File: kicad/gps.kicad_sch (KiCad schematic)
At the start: 68 parts, among them J1 Bus_PCI_Express_x1, J2 USB_C_Receptacle_USB2.0_16P, J3 Conn_01x02, J4 USB_C_Receptacle_USB2.0_16P, Q1 IRLML6344, U2 W25Q128JVP, U3 MCP25625T-E/ML, U4 RP2040, U5 NEO-M9N, X1 ABM8-272-T3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

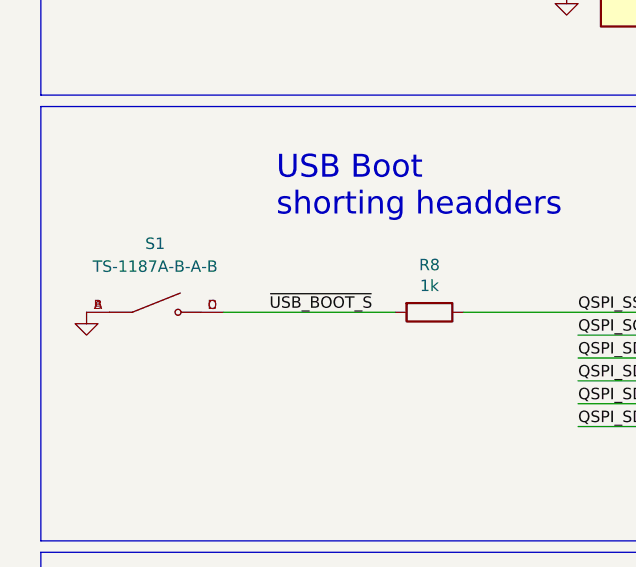
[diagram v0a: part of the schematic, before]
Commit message: Fix Battery Position
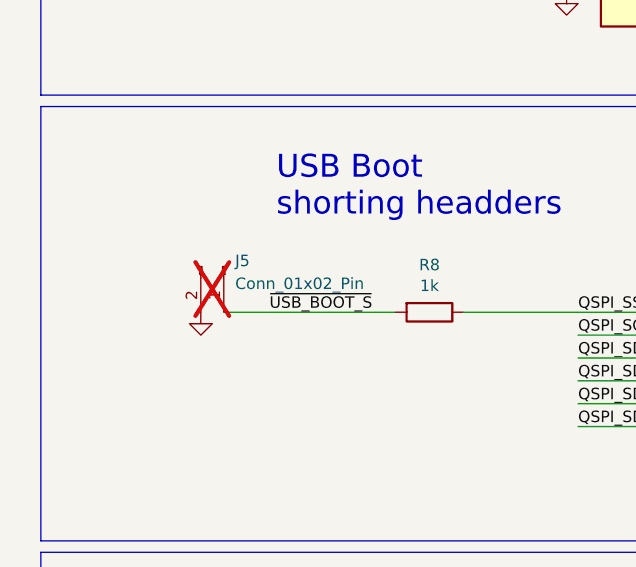
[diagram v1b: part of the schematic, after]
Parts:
- removed S1: TS-1187A-B-A-B, GPSLIB:SW_TS-1187A-B-A-B, symbol TS-1187A-B-A-B:TS-1187A-B-A-B
- added J5: Conn_01x02_Pin, Connector_PinHeader_2.54mm:PinHeader_1x02_P2.54mm_Vertical, symbol Connector:Conn_01x02_Pin
- BAT1: JLC Link https://jlcpcb.com/partdetail/C238096 -> https://jlcpcb.com/partdetail/Keystone-2998TR/C6078169; LCSC Part # C238096 -> C6078169; Manufacturer Part Number 2998 -> 2998TR
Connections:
- net GND: now also J5.2 (Pin_2)
- net ~{USB_BOOT_S}: now also J5.1 (Pin_1)

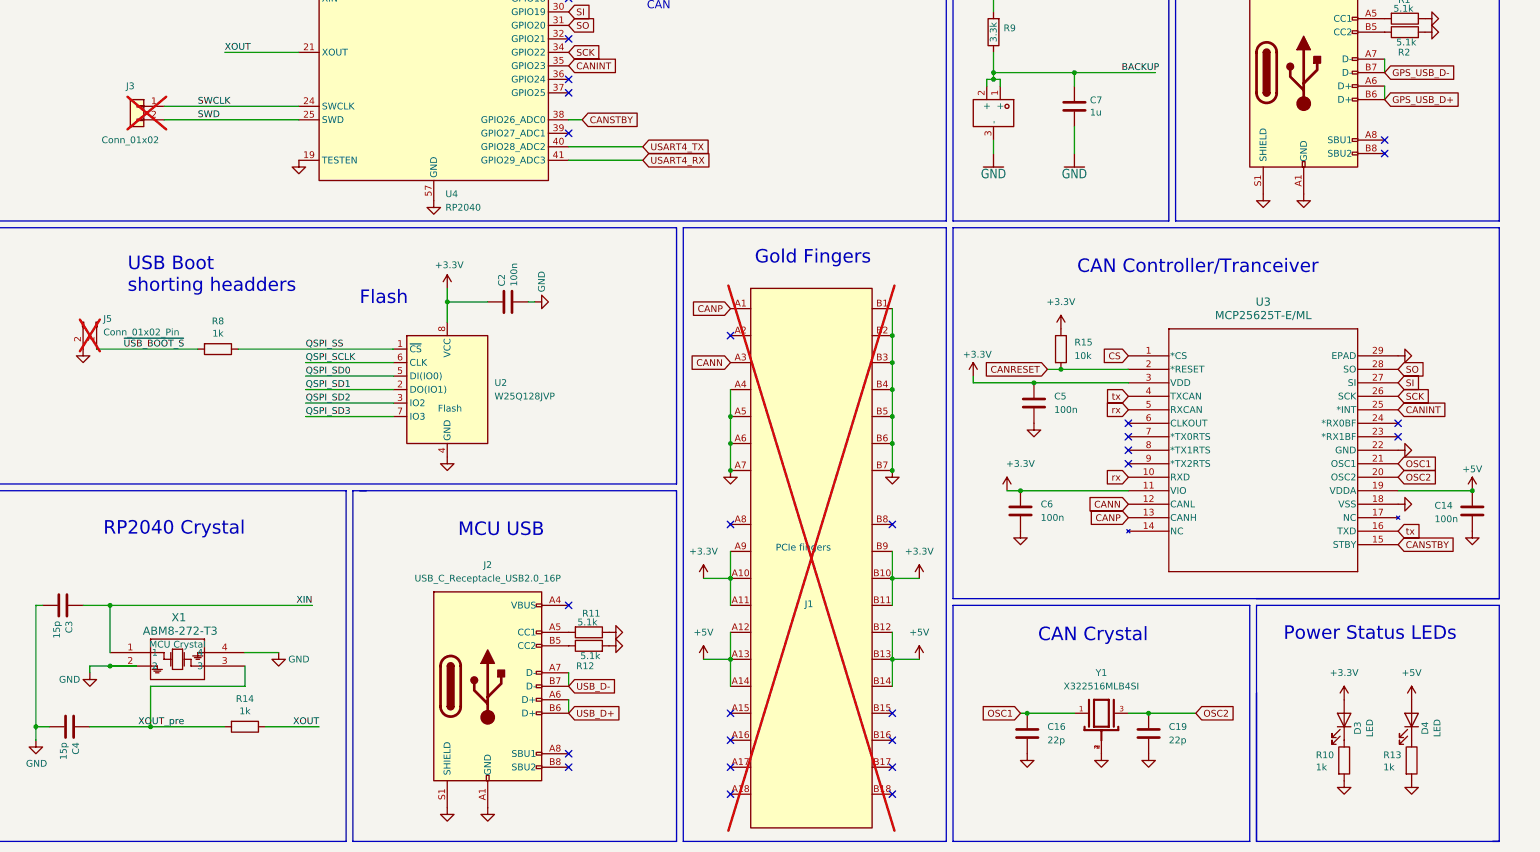
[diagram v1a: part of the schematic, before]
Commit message: Update components for order
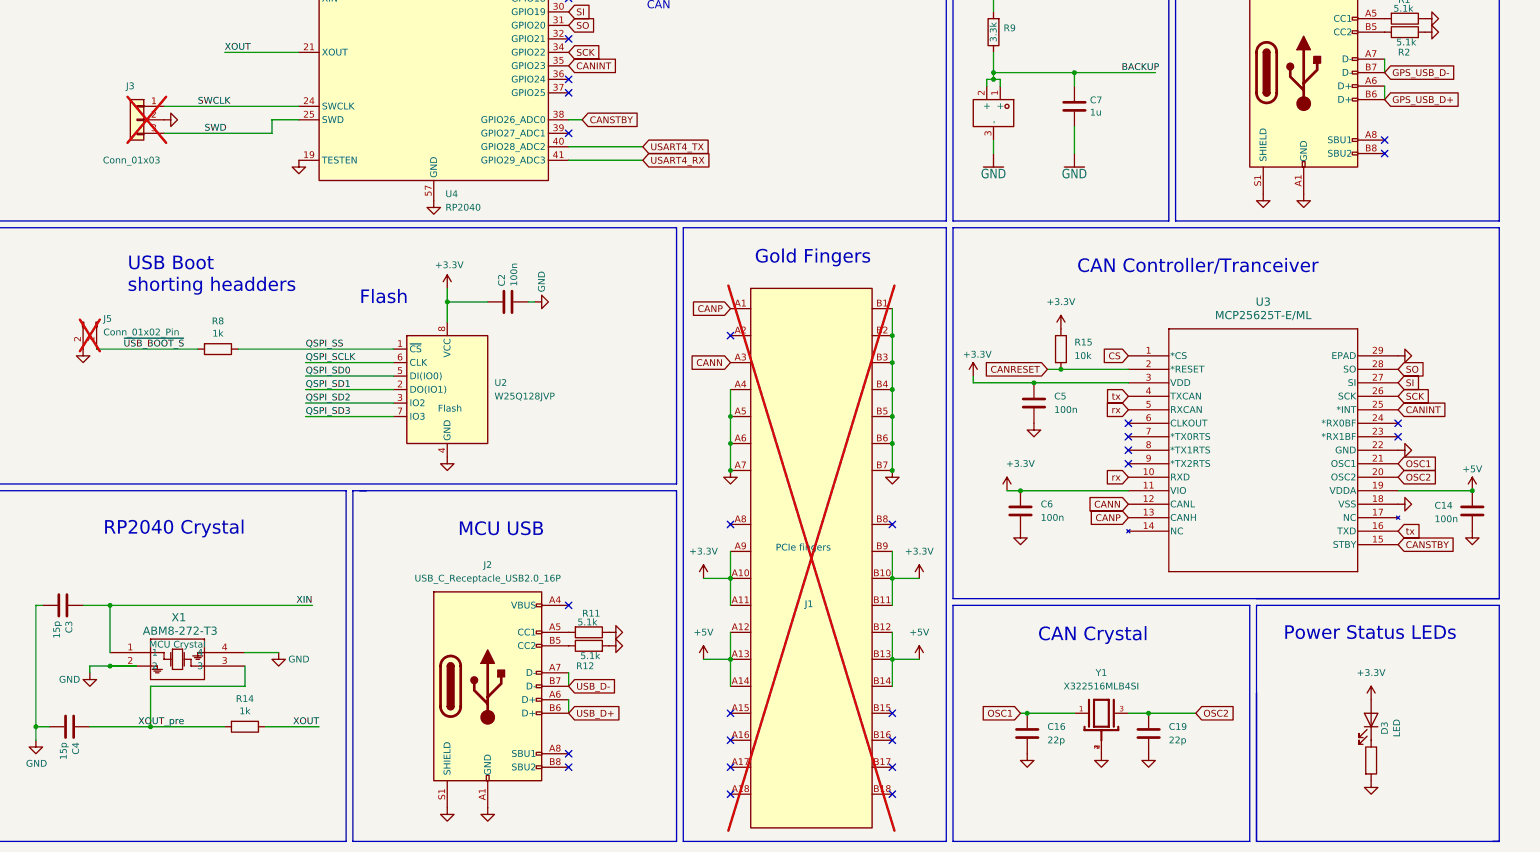
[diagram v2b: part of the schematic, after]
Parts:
- removed D4: LED, LED_SMD:LED_0603_1608Metric, symbol Device:LED
- removed R10, R13: 1k, Resistor_SMD:R_0603_1608Metric, symbol Device:R
- added R7: 1 k, Resistor_SMD:R_0603_1608Metric, symbol Device:R
- J3: value Conn_01x02 -> Conn_01x03; footprint Connector_PinHeader_2.54mm:PinHeader_1x02_P2.54mm_Vertical -> Connector_PinHeader_2.54mm:PinHeader_1x03_P2.54mm_Vertical
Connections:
- net GND: now also J3.2 (Pin_2), R7.2
- net SWD: now also J3.3 (Pin_3); no longer J3.2 (Pin_2)
- net at D3.1 (K): now also R7.1
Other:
- moved on the sheet: D3

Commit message: Final Commit before 0.2.0 Order
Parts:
- RF1: value BWSMA-KE-P001 -> BWSMA-KWE-Z001; JLC Link https://jlcpcb.com/partdetail/C496550 -> https://jlcpcb.com/partdetail/C496551; LCSC Part # C496550 -> C496551; Manufacturer Part Number BWSMA-KE-P001 -> BWSMA-KWE-Z001
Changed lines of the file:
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@@
 			)
 		)
-		(property "Value" "BWSMA-KE-P001"
+		(property "Value" "BWSMA-KWE-Z001"
 			(at 318.77 77.216 0)
 			(effects
@@
 			)
 		)
-		(property "JLC Link" "https://jlcpcb.com/partdetail/C496550"
+		(property "JLC Link" "https://jlcpcb.com/partdetail/C496551"
 			(at 317.5 68.58 0)
 			(effects
@@
 			)
 		)
-		(property "LCSC Part #" "C496550"
+		(property "LCSC Part #" "C496551"
 			(at 317.5 68.58 0)
 			(effects
@@
 			)
 		)
-		(property "Manufacturer Part Number" "BWSMA-KE-P001"
+		(property "Manufacturer Part Number" "BWSMA-KWE-Z001"
 			(at 317.5 68.58 0)
 			(effects

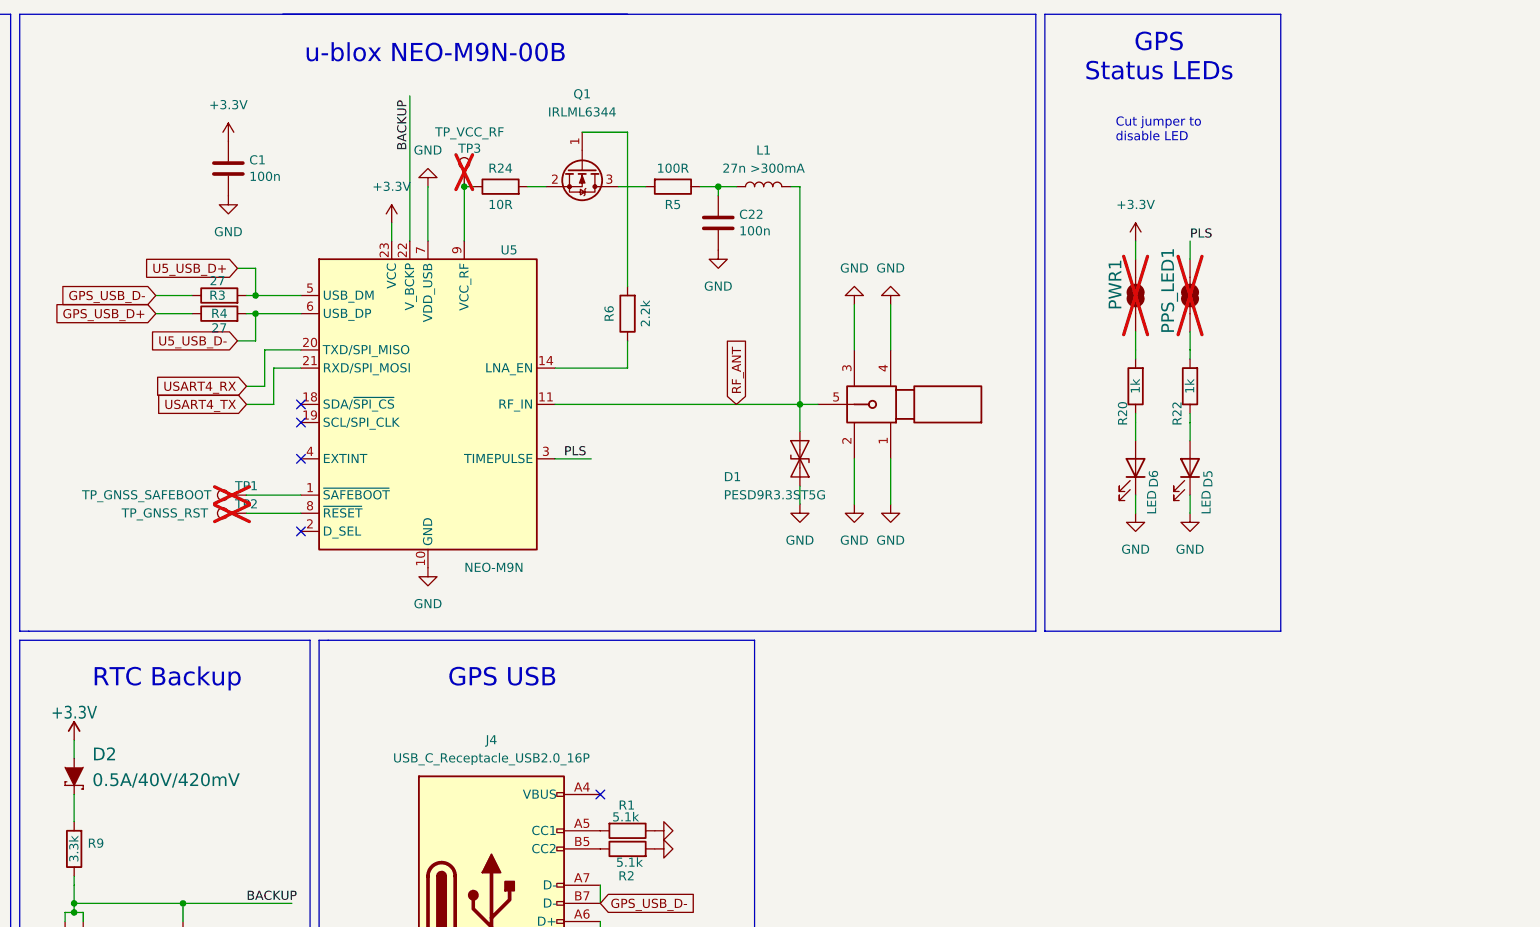
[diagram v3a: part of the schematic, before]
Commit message: Add USB detection
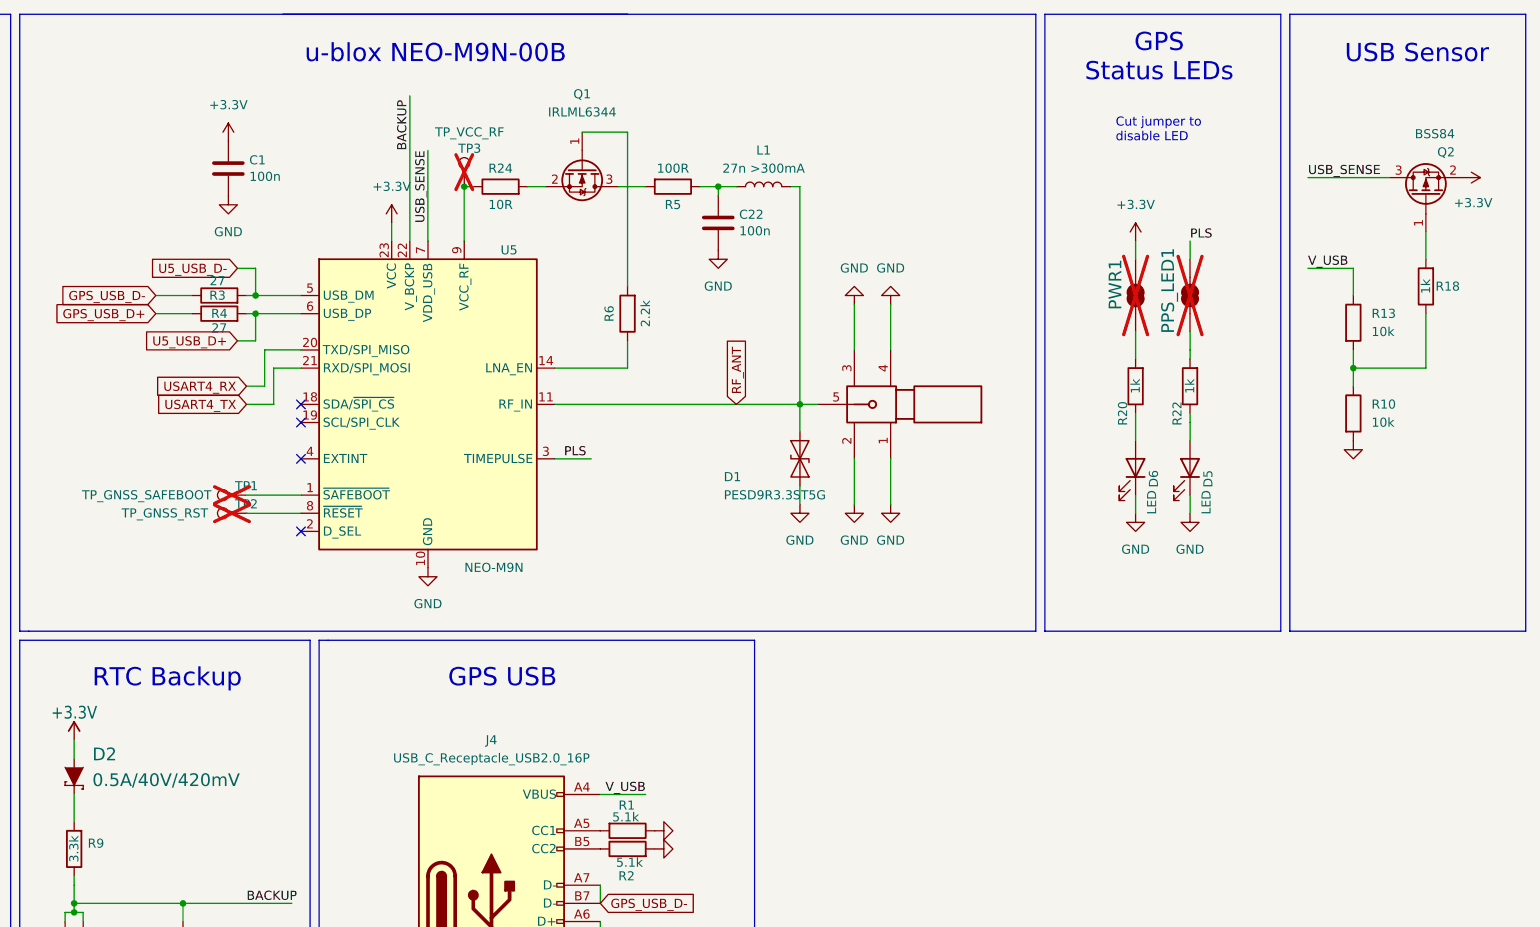
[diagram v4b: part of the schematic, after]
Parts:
- added Q2: BSS84, Package_TO_SOT_SMD:SOT-23, symbol Transistor_FET:BSS84
- added R10, R13: 10k, Resistor_SMD:R_0402_1005Metric, symbol Device:R
- added R18: 1k, Resistor_SMD:R_0402_1005Metric, symbol Device:R
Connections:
- net +3.3V: now also Q2.2 (S)
- net GND: now also R10.2; no longer U5.7 (VDD_USB)
- net U5_USB_D+: now also R4.2, U5.6 (USB_DP); no longer R3.2, U5.5 (USB_DM)
- net U5_USB_D-: now also R3.2, U5.5 (USB_DM); no longer R4.2, U5.6 (USB_DP)
- net V_USB: now reaches J4.A4 (VBUS), J4.A9 (VBUS), J4.B4 (VBUS), J4.B9 (VBUS)
- net V_USB: now also R13.1
- new net: R10.1, R13.2, R18.1
- new net: Q2.1 (G), R18.2
- new net USB_SENSE: Q2.3 (D), U5.7 (VDD_USB)
- no-connect marks 48 -> 47
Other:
- note added: "USB Sensor"

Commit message: Big Fixes
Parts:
- removed Q1: IRLML6344, Package_TO_SOT_SMD:SOT-23, symbol Transistor_FET:IRLML6244
- removed R24: 10R, Resistor_SMD:R_0402_1005Metric, symbol Device:R
- removed R6: 2.2k, Resistor_SMD:R_0402_1005Metric, symbol Device:R
- added R5: 100k, Resistor_SMD:R_0402_1005Metric, symbol Device:R
- added U1: SI1016X-T1-GE3, GPSLIB:SOT_X-T1-GE3_VIS, symbol gpsmodule:SI1016X-T1-GE3
- added U6: NC7WZ07P6X, GPSLIB:SC-88&slash_SC70-6&slash_SOT-363_419B-02_ONS, symbol gpsmodule:NC7WZ07P6X
- R5: value 100R -> 10R; Info Thick Film Chip Resistor, 100 Ω, 0402 package, ±1% toleranc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 -> -55℃~+155℃ 10Ω 50V 62.5mW Thick Film Resistor ±1% ±200ppm/℃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; JLC Link https://jlcpcb.com/partdetail/25821-0402WGF1000TCE/C25078 -> https://jlcpcb.com/partdetail/25820-0402WGF100JTCE/C25077; LCSC Part # C25078 -> C25077; Manufacturer Part Number 0402WGF1000TCE -> 0402WGF100JTCE
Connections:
- net GND: now also U1.1 (S1)
- net VCC_RF: now reaches TP3.1, U5.9 (VCC_RF)
- net VCC_RF: now also R5.2, U1.4 (S2)
- net BIAS_T: now reaches R5.2
- net BIAS_T: now also U1.3 (D2)
- net LNA_EN: now reaches U5.14 (LNA_EN)
- net LNA_EN: now also U1.2 (G1)
- new net: R5.1, U1.5 (G2), U1.6 (D1)

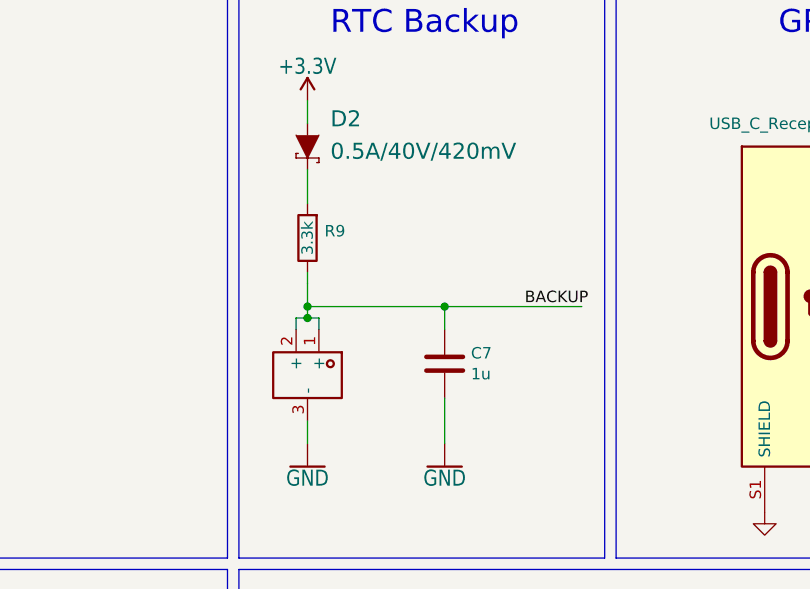
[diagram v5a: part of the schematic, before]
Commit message: Add Supercap
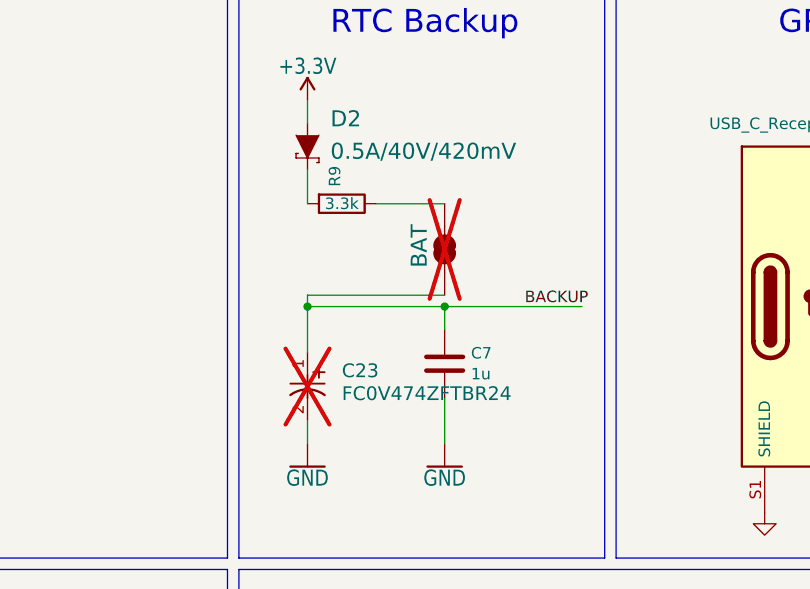
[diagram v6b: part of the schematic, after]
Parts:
- removed BAT1: 2998, BAT-SMD_C238096, symbol gpsmodule:2998
- added BAT: JUMPER-SMT_2_NC_TRACE_SILK, GPSLIB:SMT-JUMPER_2_NC_TRACE_SILK, symbol SparkFun u-blox GNSS MAX-M10S-eagle-import:JUMPER-SMT_2_NC_TRACE_SILK
- added C23: FC0V474ZFTBR24, GPSLIB:FC0V474ZFTBR24_KEM, symbol gpsmodule:FC0V474ZFTBR24
- U1: Basic Part? (none) -> Yes; Current Draw (none) -> N/A (controlled by gate; I<sub>D</sub> max = -0.82 A); Info (none) -> -55℃~+150℃ 1 N-Channel + 1 P-Channel 1V@250uA 2.7Ω@1.8V,150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; JLC Link (none) -> https://jlcpcb.com/partdetail/VishayIntertech-SI1016X_T1GE3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; LCSC Part # (none) -> C142570; Manufacturer Name (none) -> Vishay Intertech; Manufacturer Part Number (none) -> SI1016X-T1-GE3; Price (none) -> C$0.0418 (1+)
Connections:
- net BACKUP: now also BAT.1, C23.1; no longer R9.1
- net GND: now also C23.2
- new net: BAT.2, R9.1
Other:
- moved on the sheet: R9

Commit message: U6
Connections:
- net GND: now also U6.2 (GND)
- net VCC_RF: now also U6.5 (VCC)
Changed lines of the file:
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@@
 	(wire
 		(pts
+			(xy 381 215.9) (xy 374.65 215.9)
+		)
+		(stroke
+			(width 0)
+			(type default)
+		)
+	)
+	(wire
+		(pts
 			(xy 100.33 179.07) (xy 100.33 181.61)
 		)
@@
 		)
 	)
+	(label "VCC_RF"
+		(at 381 215.9 0)
+		(effects
+			(font
+				(size 1.27 1.27)
+			)
+			(justify left bottom)
+		)
+	)
 	(label "QSPI_SD1"
 		(at 73.66 198.12 0)
@@
 					(unit 1)
 				)
+			)
+		)
+	)
+	(symbol
+		(lib_id "power:GND")
+		(at 334.01 215.9 270)
+		(unit 1)
+		(exclude_from_sim no)
+		(in_bom yes)
+		(on_board yes)
+		(dnp no)
+		(fields_autoplaced yes)
+		(property "Reference" "#PWR063"
+			(at 327.66 215.9 0)
+			(effects
+				(font
+					(size 1.27 1.27)
+				)
+				(hide yes)
+			)
+		)
+		(property "Value" "GND"
+			(at 328.93 215.9 0)
+			(effects
+				(font
+					(size 1.27 1.27)
+				)
+				(hide yes)
+			)
+		)
+		(property "Footprint" ""
+			(at 334.01 215.9 0)
+			(effects
+				(font
+					(size 1.27 1.27)
+				)
+				(hide yes)
+			)
+		)
+		(property "Datasheet" ""
+			(at 334.01 215.9 0)
+			(effects
+				(font
+					(size 1.27 1.27)
+				)
+				(hide yes)
+			)
+		)
+		(property "Description" "Power symbol creates a global label with name \"GND\" , ground"
+			(at 334.01 215.9 0)
+			(effects
+				(font
+					(size 1.27 1.27)
+				)
+				(hide yes)
+			)
+		)
+		(pin "1"
+		)
+		(instances
+			(project "gps"
+				(path "/e1ff46b9-0cf9-4507-8034-1e95fc3013fc"
+					(reference "#PWR063")
+					(unit 1)
+				)
